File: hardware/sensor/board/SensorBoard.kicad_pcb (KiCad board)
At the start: 4 copper layers, 40 x 25 mm, 36 parts, among them J1 USB_B_Mini, J2 Conn_01x04_Male, U1 93LC56BT-I/OT, U2 FT232H, U3 74LVC2G17, U4 74LVC1G374, U5 74LVC1G04, Y1 12MHz

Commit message: Update SensorBoard.kicad_pcb
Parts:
- added R7: 1k, Resistor_SMD:R_0603_1608Metric, F.Cu at (128.8, 91.3)
- added WR#: LED, LED_SMD:LED_0603_1608Metric, F.Cu at (128.1, 89.1)
- C1, C3: value .1uF -> 0.1uF; footprint Capacitor_SMD:C_0805_2012Metric -> Capacitor_SMD:C_0603_1608Metric
- C10, C11, C12, C13, C14, C15, C2, C4, C5, C6, C7, C8, C9: footprint Capacitor_SMD:C_0805_2012Metric -> Capacitor_SMD:C_0603_1608Metric
- D1, D2: footprint Diode_SMD:D_0805_2012Metric -> Diode_SMD:D_0603_1608Metric
- FB1, FB2, FB3: footprint Inductor_SMD:L_0805_2012Metric -> Inductor_SMD:L_0603_1608Metric
- J2: footprint Connector_PinHeader_1.00mm:PinHeader_1x04_P1.00mm_Vertical -> Connector_PinHeader_2.54mm:PinHeader_1x04_P2.54mm_Vertical
- R1, R2, R3, R4, R5, R6, R8, R9: footprint Resistor_SMD:R_0805_2012Metric -> Resistor_SMD:R_0603_1608Metric
- Y1: footprint Crystal:Crystal_SMD_2016-4Pin_2.0x1.6mm -> Crystal:Crystal_SMD_2520-4Pin_2.5x2.0mm
- moved U3 135.8 mm to (130.8, 95.9), turned to 180 degrees
- moved U4 132.6 mm to (123.1, 95.9), turned to 90 degrees
- moved U1 132.1 mm to (132.2, 83.5), turned to 90 degrees
- moved C1 131.6 mm to (131.2, 79.9)
- moved R2 131.4 mm to (132.2, 86.1), turned to 180 degrees
- moved U5 129.5 mm to (126.9, 95.9), turned to 90 degrees
- moved R3 126.8 mm to (113.7, 84.8)
- moved R1 126.7 mm to (128.1, 86.1), turned to 0 degrees
- moved C5 126.5 mm to (110.0, 78.4)
- moved FB2 126.2 mm to (112.3, 81.8)
- moved FB1 126.1 mm to (111.5, 78.4)
- moved C7 125.9 mm to (112.3, 83.3)
- moved J1 125.5 mm to (105.4, 87.5)
- moved C12 125.3 mm to (126.0, 92.6), turned to 0 degrees
- moved C2 125.1 mm to (117.8, 79.5), turned to 270 degrees
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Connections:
- net Net-(C2-Pad1) renamed /CLK+
- net Net-(C3-Pad1) renamed /VCCA
- net Net-(C4-Pad1) renamed /CLK-
- net Net-(J2-Pad2) renamed /Phase1
- net Net-(J2-Pad3) renamed /Phase2
- net Net-(R3-Pad1) renamed /REF
- net Net-(R4-Pad1) renamed /RESET
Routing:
- net VCC3V3: track 116.4 -> 35.8 mm, vias 9 -> 11
- net VBUS: track 63.4 -> 10.4 mm
- net Net-(J1-Pad6): track 0.00 -> 19.8 mm
- net EECS: track 6.52 -> 24.8 mm
- net GND: track 87.9 -> 71.5 mm, vias 25 -> 28
- net EECLK: track 7.63 -> 20.7 mm
- net /Phase2: track 18.7 -> 8.81 mm
- net VCORE: track 14.4 -> 4.99 mm
- net /VCCA: track 13.9 -> 4.76 mm
- net EEDATA: track 15.6 -> 23.0 mm
- net WR#: track 15.2 -> 8.03 mm
- net VPHY: track 12.1 -> 6.32 mm
- net /REF: track 9.18 -> 3.38 mm
- net /RESET: track 7.26 -> 2.16 mm
- net Net-(U3-Pad6): track 1.82 -> 6.31 mm
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- added copper zone on F.Cu, net GND
- added copper zone on In1.Cu, net GND
- added copper zone on B.Cu, net VBUS
- added copper zone on In2.Cu, net VCC3V3
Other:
- net class Default: clearance 0.2 -> 0.127
- net class USB removed
- rule pad_to_mask_clearance: 0 -> 0.0508
- rule trace_clearance: 0.2 -> 0.127
- rule trace_min: 0.2 -> 0.127
- rule via_min_drill: 0.3 -> 0.254
- rule via_min_size: 0.4 -> 0.4572
- board text added: "Rev 0.5"

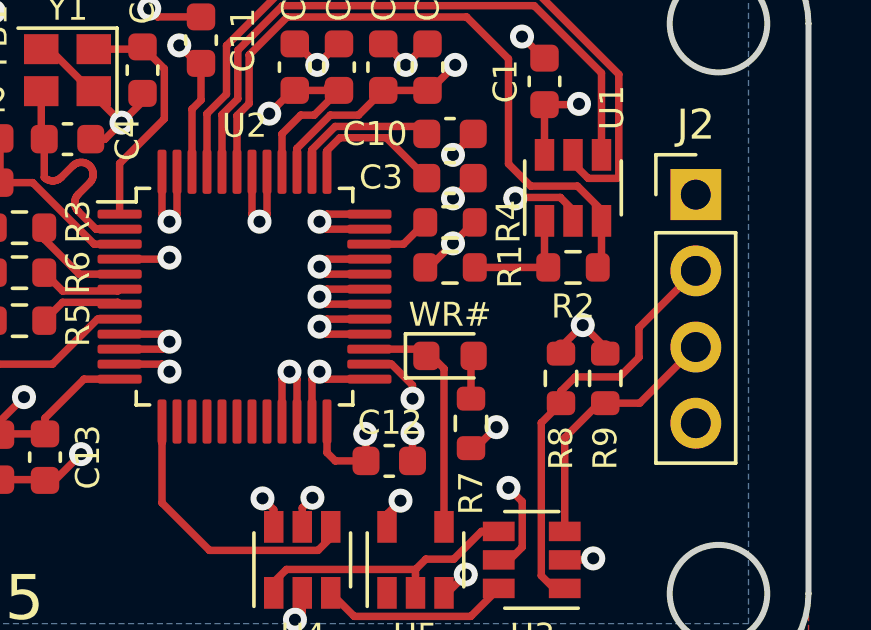
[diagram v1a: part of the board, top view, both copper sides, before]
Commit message: Fixing planes and debug LED
Fixing some planes, via off of the debug LED
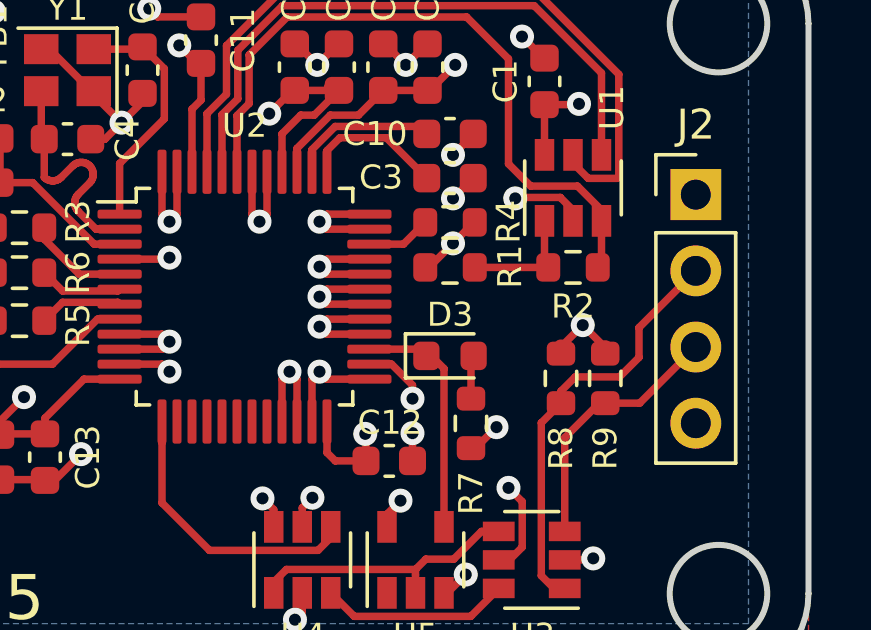
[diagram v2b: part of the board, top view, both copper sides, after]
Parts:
- renumbered WR# to D3
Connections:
- R7 pad 2: VCCV3 -> VCC3V3
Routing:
- net VCCV3: track 1.14 -> 0.00 mm, vias 1 -> 0
- net VCC3V3: track 35.8 -> 36.9 mm, vias 11 -> 12

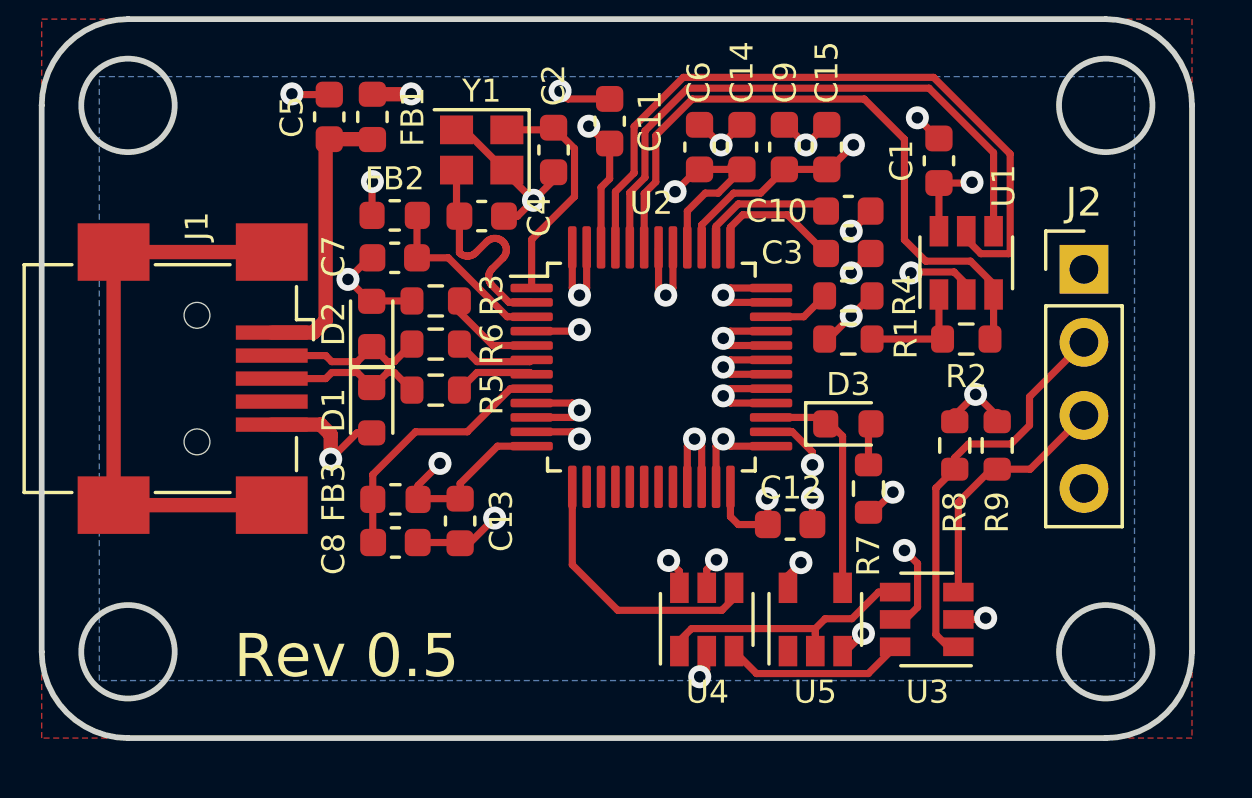
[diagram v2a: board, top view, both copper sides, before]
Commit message: Added power status LEDs
Rev'd board to 0.6, added power status LEDs for 5V and 3V3 rails to help debug
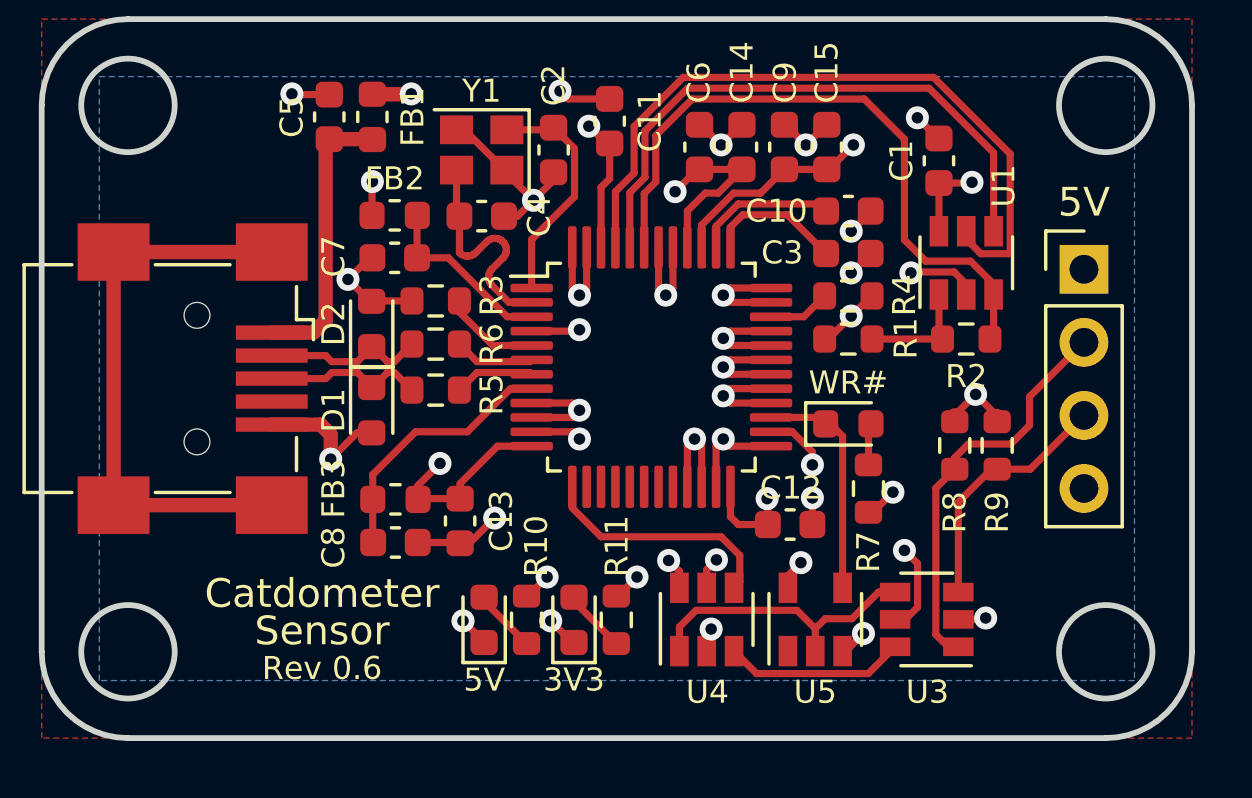
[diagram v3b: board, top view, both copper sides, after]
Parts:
- removed D3: LED, LED_SMD:LED_0603_1608Metric
- added 3V3: ORANGE, LED_SMD:LED_0603_1608Metric, F.Cu at (118.5, 95.9)
- added 5V: GREEN, LED_SMD:LED_0603_1608Metric, F.Cu at (115.4, 95.9)
- added R10: 580, Resistor_SMD:R_0603_1608Metric, F.Cu at (116.9, 95.9)
- added R11: 240, Resistor_SMD:R_0603_1608Metric, F.Cu at (120.0, 95.9)
- added WR#: GREEN, LED_SMD:LED_0603_1608Metric, F.Cu at (128.1, 89.1)
- turned R7 to 90 degrees
- renumbered J2 to 5V
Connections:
- R7 pad 1: Net-(D3-Pad2) -> VCC3V3
- R7 pad 2: VCC3V3 -> Net-(D3-Pad2)
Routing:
- net Net-(D4-Pad2): track 0.00 -> 2.22 mm
- net Net-(D5-Pad2): track 0.00 -> 2.22 mm
- net GND: track 71.5 -> 73.5 mm, vias 28 -> 30
- net Net-(U3-Pad4): track 9.34 -> 10.5 mm
- net VCC3V3: track 36.9 -> 37.9 mm, vias 12 -> 13
- net VBUS: track 10.4 -> 11.4 mm, vias 3 -> 4
- net DIR: track 10.2 -> 9.51 mm
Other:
- board text added: "Catdometer"
- board text added: "Rev 0.6"
- board text added: "Sensor"
- board text removed: "Rev 0.5"

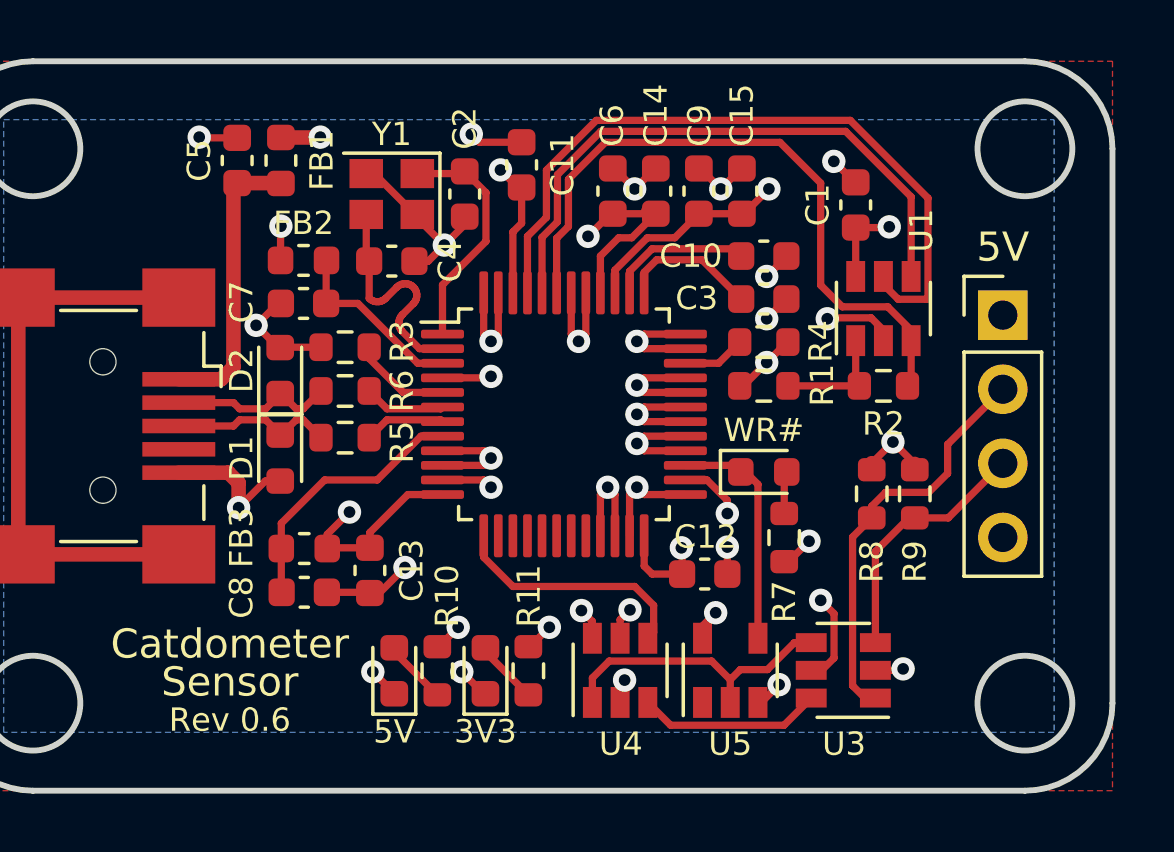
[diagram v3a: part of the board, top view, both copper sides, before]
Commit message: Board relayout
Some relayout of the southern and eastern side of the board, addition of DIR LED, moving WR down to be with the rest.
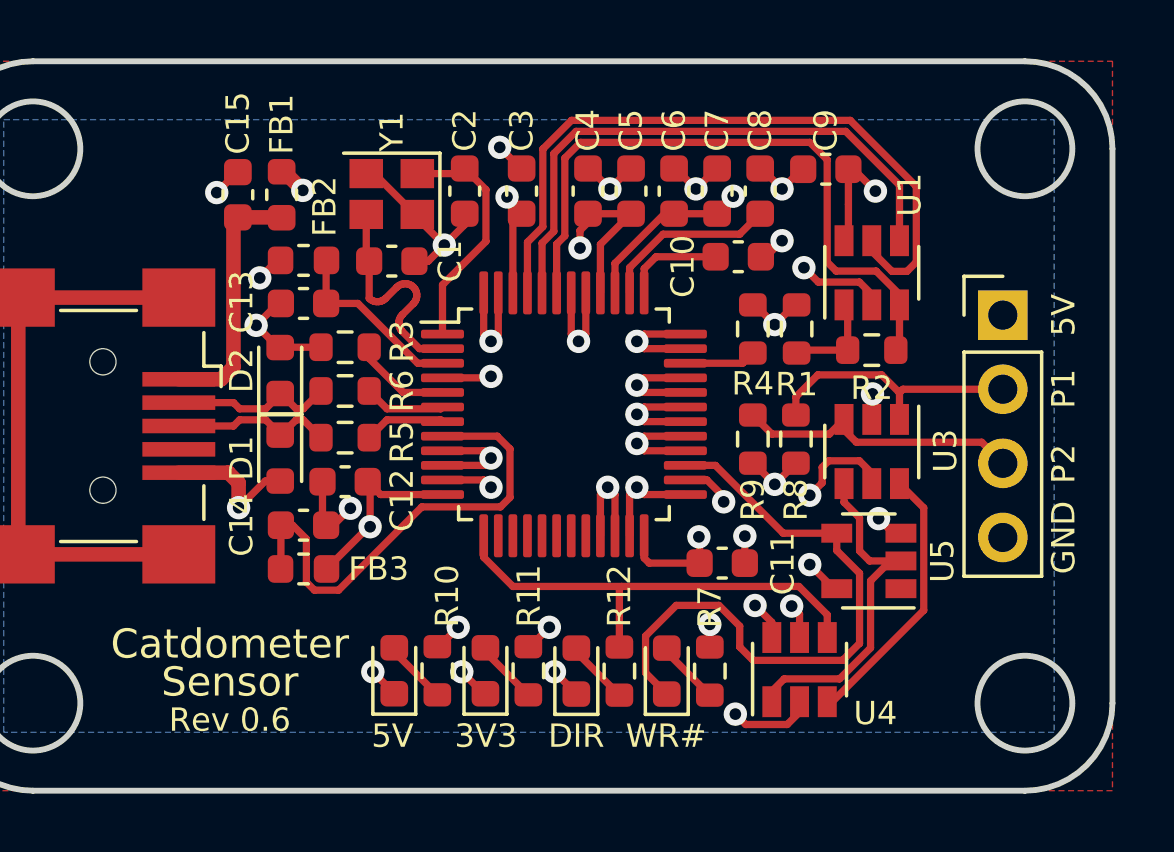
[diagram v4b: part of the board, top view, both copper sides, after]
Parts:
- removed the C12 at (126.0, 92.6)
- added C11: 0.1uF, Capacitor_SMD:C_0603_1608Metric, F.Cu at (126.6, 92.2)
- added LED_DIR1: GREEN, LED_SMD:LED_0603_1608Metric, F.Cu at (121.6, 95.9)
- added R12: 240, Resistor_SMD:R_0603_1608Metric, F.Cu at (123.1, 95.9)
- R7: value 1k -> 240
- moved LED_WR#1 7.59 mm to (124.7, 95.9), turned to 90 degrees
- moved U3 7.56 mm to (131.8, 88.4), turned to 270 degrees
- moved U4 6.15 mm to (129.3, 95.8)
- moved U5 6.05 mm to (131.7, 92.1), turned to 180 degrees
- moved R9 5.86 mm to (127.7, 88.0), turned to 90 degrees
- moved R7 5.24 mm to (126.2, 95.9), turned to 270 degrees
- moved R8 3.21 mm to (129.2, 88.0), turned to 90 degrees
- moved C12 3.16 mm to (113.7, 89.4), turned to 180 degrees
- moved C14 2.30 mm to (112.3, 90.9)
- moved R1 2.25 mm to (129.2, 84.2), turned to 270 degrees
- moved C8 2.23 mm to (127.9, 79.5), turned to 90 degrees
- moved C10 1.69 mm to (127.2, 81.7)
- moved C9 1.60 mm to (130.2, 78.7), turned to 180 degrees
- moved R2 1.29 mm to (131.8, 84.9)
- moved U1 1.29 mm to (131.8, 82.2)
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- renumbered C4 to C1, C3 to C10, C13 to C12, C7 to C13, C8 to C14, C5 to C15, C11 to C3, C6 to C4, C14 to C5, C9 to C6, C15 to C7, C10 to C8, C1 to C9, 5V to J2, 3V3 to LED_3V3, 5V to LED_5V0, WR# to LED_WR#1
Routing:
- net WR#: track 8.03 -> 21.7 mm
- net VPLL: track 9.13 -> 16.6 mm
- net DIR: track 9.51 -> 16.9 mm
- net /Phase1: track 14.1 -> 9.25 mm
- net Net-(U3-Pad6): track 6.31 -> 9.29 mm
- net GND: track 73.5 -> 75.8 mm
- net Net-(LED_DIR1-Pad2): track 0.00 -> 2.22 mm
- net VCC3V3: track 37.9 -> 36.0 mm
- net Net-(U3-Pad4): track 10.5 -> 12.1 mm
- net VBUS: track 11.4 -> 9.97 mm
- net /VCCA: track 4.76 -> 3.45 mm
- net Net-(C15-Pad1): track 9.91 -> 8.73 mm
- net VCORE: track 4.99 -> 6.10 mm
- net /Phase2: track 8.81 -> 9.88 mm
- net EECLK: track 20.7 -> 19.8 mm
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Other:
- board text added: "3V3"
- board text added: "5V"
- board text added: "DIR"
- board text added: "GND"
- board text added: "P1"
- board text added: "P2"
- board text added: "WR#"

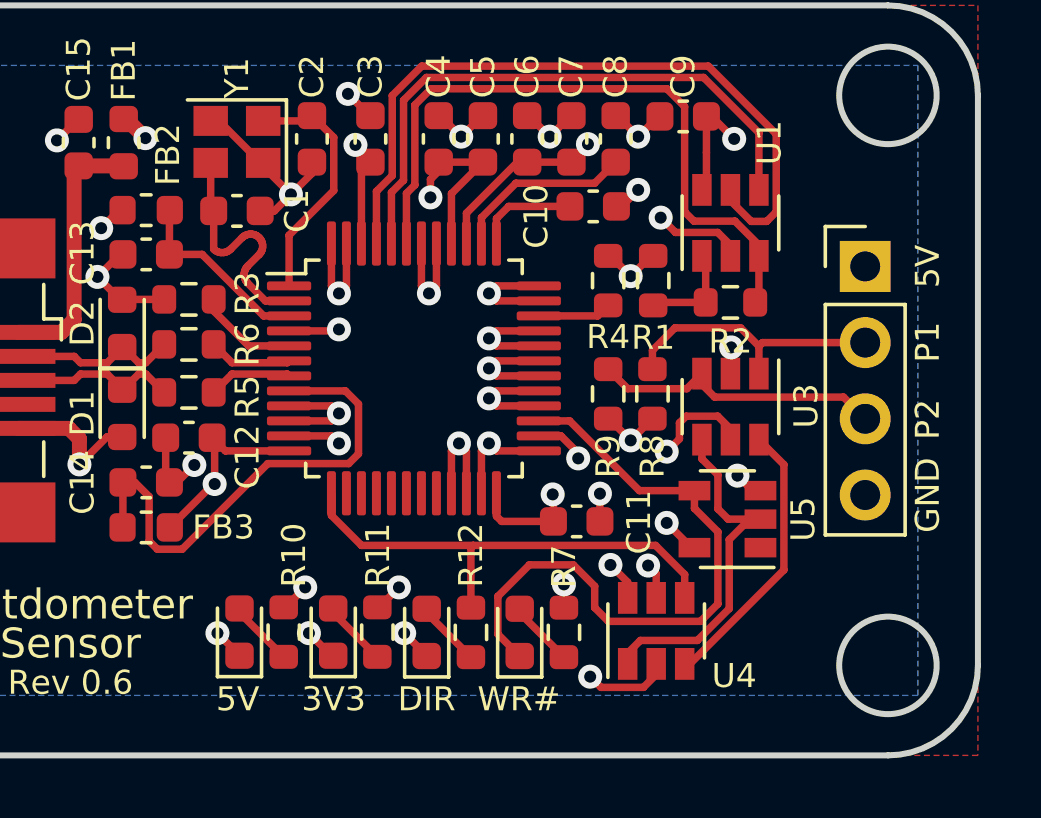
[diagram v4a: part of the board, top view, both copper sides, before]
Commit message: Reordering of resistors
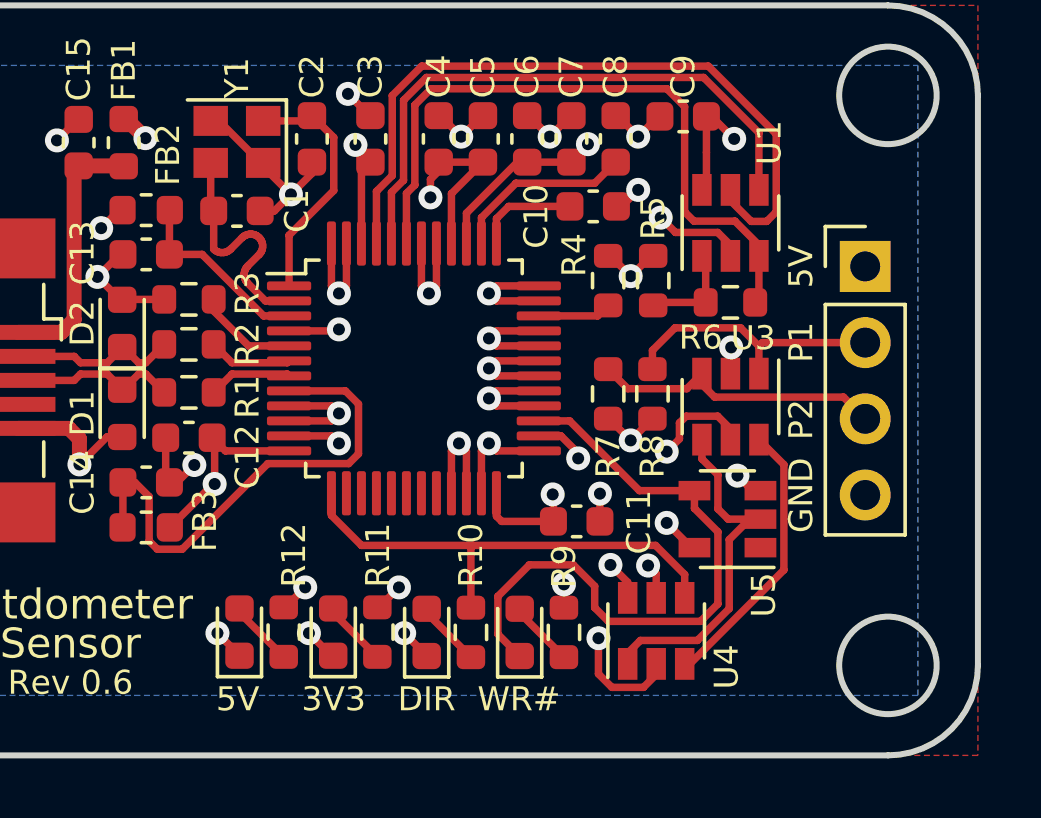
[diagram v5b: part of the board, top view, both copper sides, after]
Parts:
- renumbered R5 to R1, R12 to R10, R10 to R12, R6 to R2, R1 to R5, R2 to R6, R9 to R7, R7 to R9
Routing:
- net GND: track 75.8 -> 76.8 mm
